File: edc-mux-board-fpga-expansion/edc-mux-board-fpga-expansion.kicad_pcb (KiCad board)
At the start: 4 copper layers, 224.5 x 177.5 mm, 375 parts, among them J1 DD-78F, J2 Device 8, J3 Device 9, J4 Device 10, J5 Device 11, J6 Device 12, J7 Device 13, J8 Device 14, J9 Device 15, U1 EP5358HUI, U10 TLV320AIC3206, U11 FSA2367, U12 P82B96, U13 TLV320AIC3206, U14 FSA2367, U15 P82B96, U16 TLV320AIC3206, U17 FSA2367, U18 P82B96, U19 TLV320AIC3206, U2 R-78B3.3-2.0, U20 FSA2367, U21 P82B96, U22 TLV320AIC3206, U23 FSA2367, U24 P82B96, U25 TLV320AIC3206, U26 FSA2367, U27 CDCLVC1108, U28 TCA9555RTWR, U29 TCA9548A, U3 P82B96, U4 TLV320AIC3206, U5 FSA2367, U6 P82B96, U7 TLV320AIC3206, U8 FSA2367, U9 P82B96

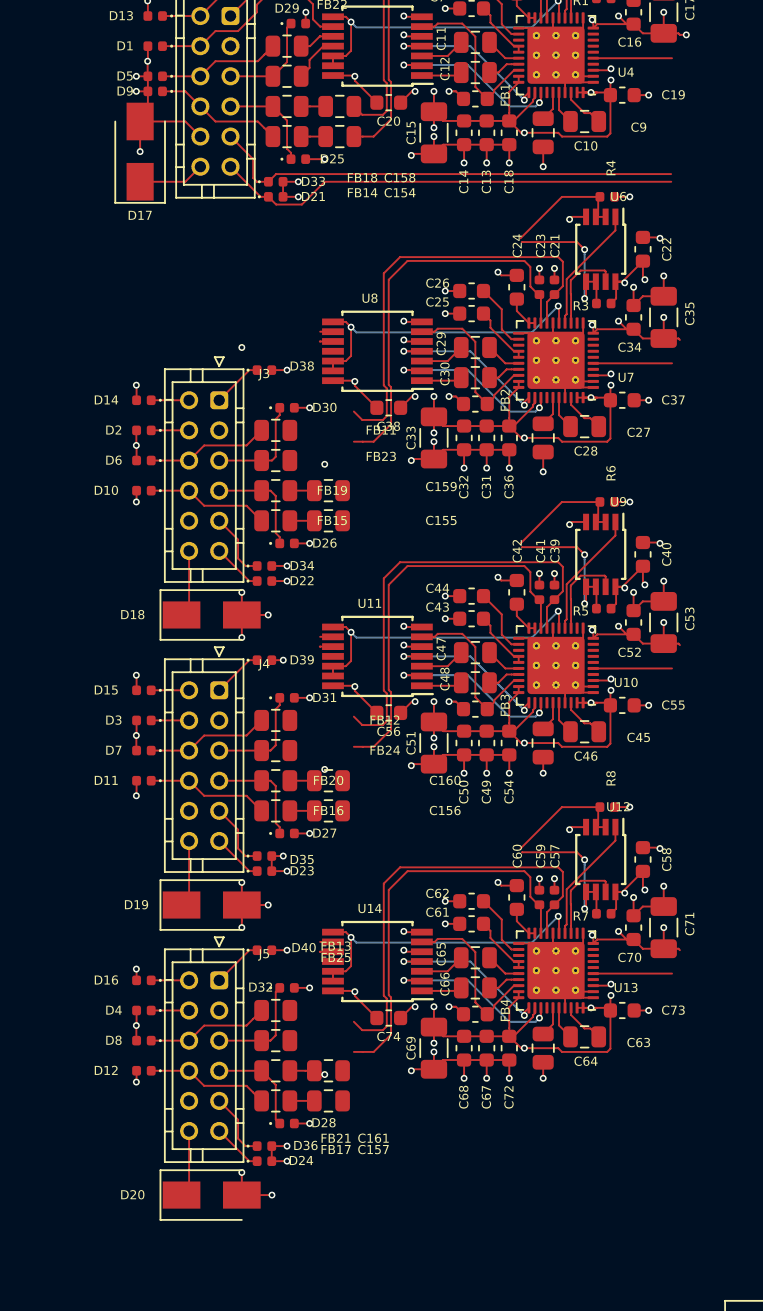
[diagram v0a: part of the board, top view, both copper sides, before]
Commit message: more pcb work. working on left side connector positioning
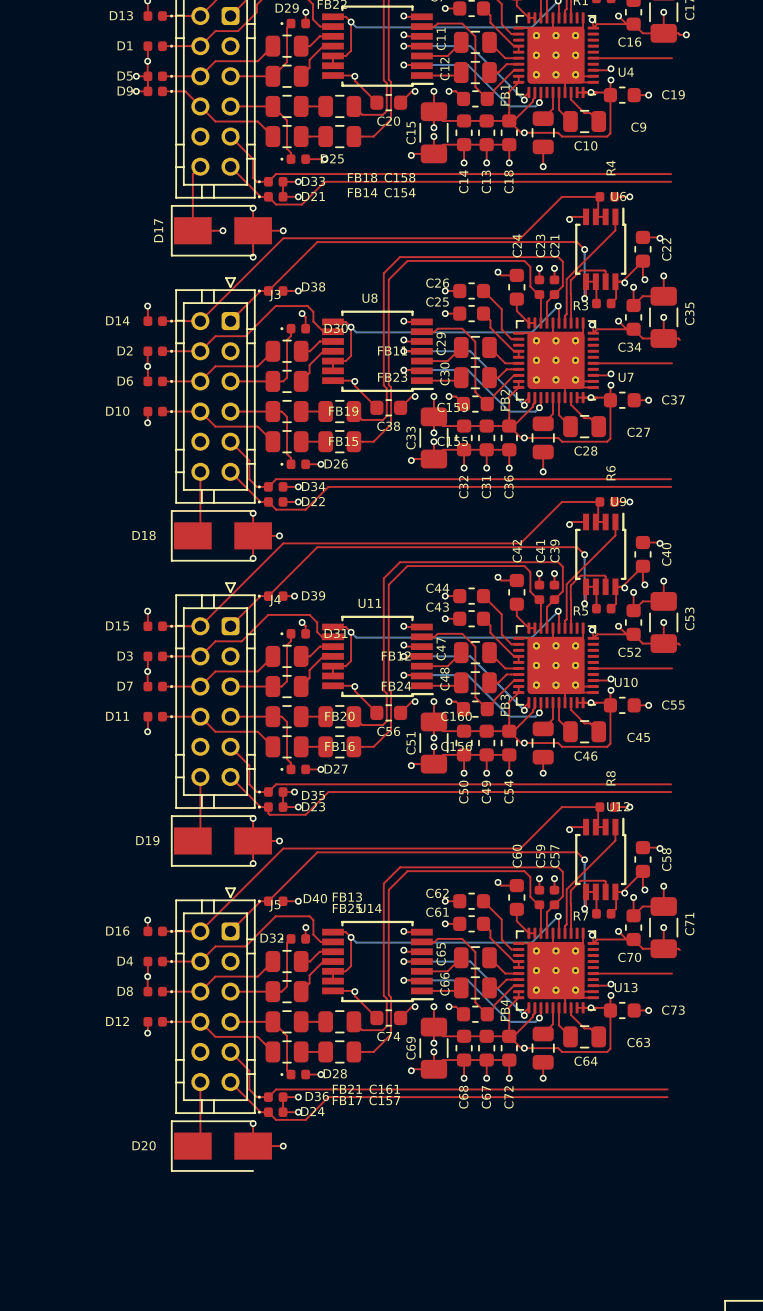
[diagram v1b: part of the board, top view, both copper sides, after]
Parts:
- moved D17 7.60 mm to (108.5, 64.8), turned to 0 degrees
- moved C155 5.30 mm to (116.2, 78.8)
- moved C159 5.30 mm to (116.2, 76.8)
- moved D10 5.30 mm to (104.0, 76.8)
- moved D14 5.30 mm to (104.0, 70.8)
- moved D18 5.30 mm to (108.5, 85.0)
- moved D2 5.30 mm to (104.0, 72.8)
- moved D22 5.30 mm to (112.0, 82.8)
- moved D26 5.30 mm to (113.5, 80.2)
- moved D30 5.30 mm to (113.5, 71.2)
- moved D34 5.30 mm to (112.0, 81.8)
- moved D38 5.30 mm to (112.0, 68.8)
- moved D6 5.30 mm to (104.0, 74.8)
- moved FB11 5.30 mm to (112.8, 72.8)
- moved FB15 5.30 mm to (112.8, 78.8)
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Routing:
- net /Left Side Connector Interconnects/ID_PIN10: track 3.34 -> 31.2 mm
- net /Left Side Connector Interconnects/ID_PIN9: track 3.34 -> 30.9 mm
- net /Left Side Connector Interconnects/ID_PIN11: track 3.34 -> 30.7 mm
- net /Left Side Connector Interconnects/INT_9: track 4.49 -> 31.4 mm
- net /Left Side Connector Interconnects/INT_10: track 4.49 -> 31.4 mm
- net /Left Side Connector Interconnects/INT_11: track 4.49 -> 31.2 mm
- net /CODEC interconnection sheet/SDA_HV9: track 10.8 -> 34.4 mm
- net /CODEC interconnection sheet/SDA_HV11: track 10.8 -> 34.4 mm
- net /CODEC interconnection sheet/SDA_HV10: track 10.8 -> 34.4 mm
- net /CODEC interconnection sheet/SCL_HV11: track 14.2 -> 32.4 mm
- net /CODEC interconnection sheet/SCL_HV10: track 14.2 -> 32.4 mm
- net /CODEC interconnection sheet/SCL_HV9: track 14.2 -> 32.4 mm
- net /CODEC interconnection sheet/AUD_GND11: track 3.37 -> 13.8 mm
- net /CODEC interconnection sheet/AUD_GND9: track 3.37 -> 13.6 mm
- net /CODEC interconnection sheet/AUD_GND10: track 3.37 -> 13.4 mm
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
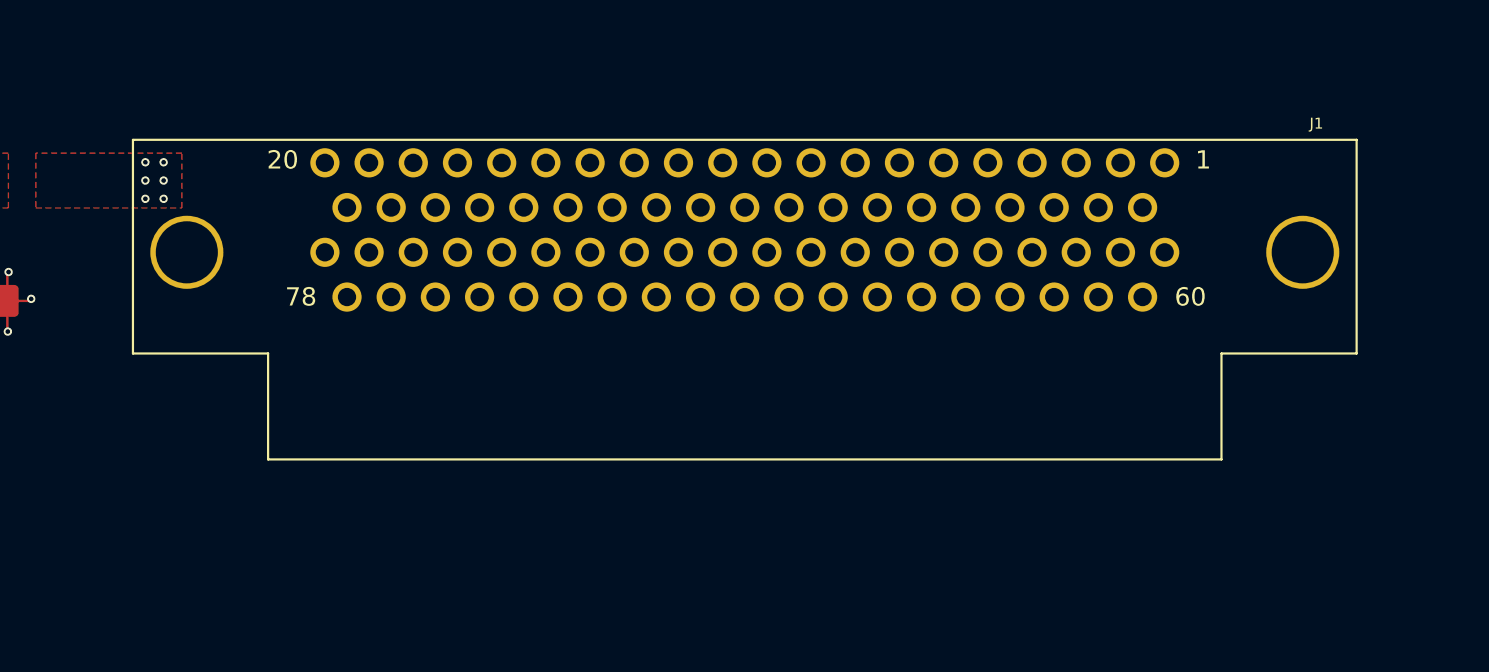
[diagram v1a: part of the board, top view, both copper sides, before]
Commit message: Changed expansion connector from DD-78 to DC-62
since the connector is literally half as much, and I don't need the extra pins
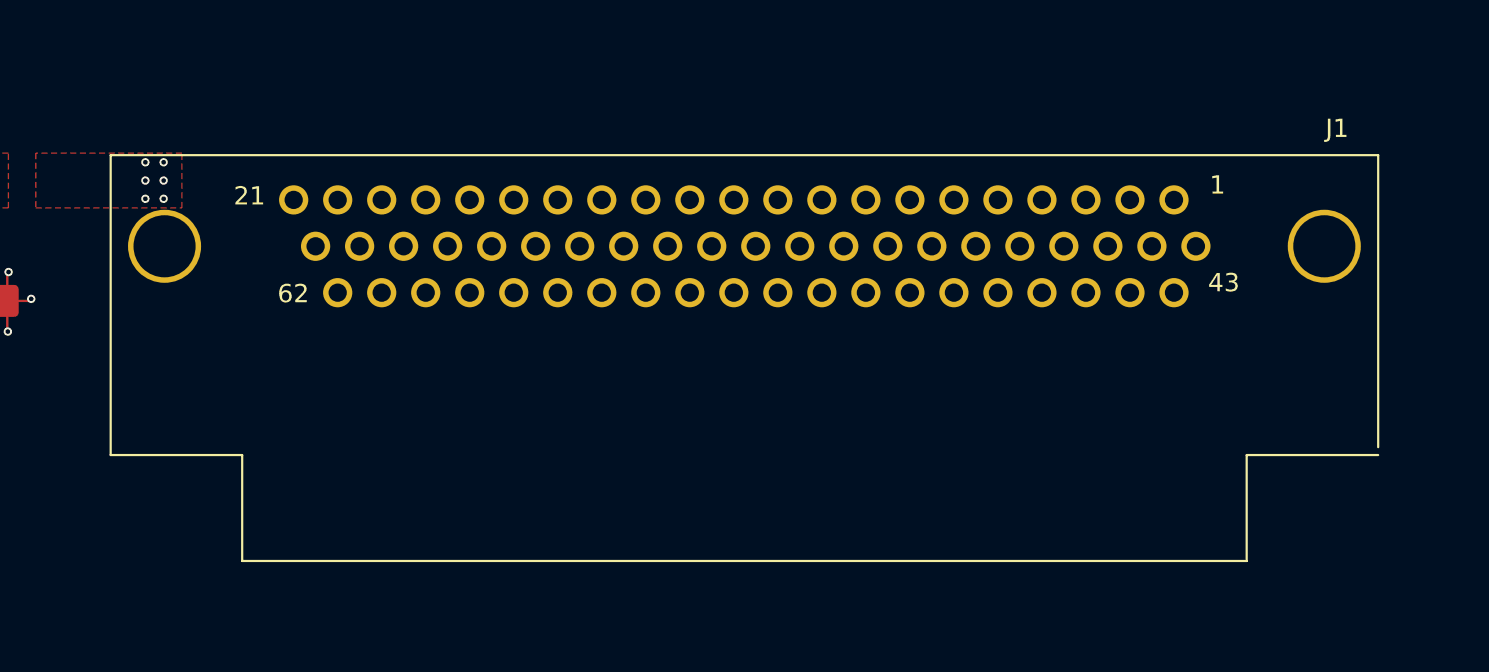
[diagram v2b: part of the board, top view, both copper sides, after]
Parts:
- J1: value DD-78F -> DC-62F; footprint SW-Harting:09565525612 -> SW-Harting:09564525612
- moved J1 2.78 mm to (175.3, 141.6)
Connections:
- J1 pad 1: (no net) -> Net-(J1-Pad1)
- J1 pad 10: (no net) -> Net-(J1-Pad10)
- J1 pad 11: (no net) -> Net-(J1-Pad11)
- J1 pad 12: (no net) -> Net-(J1-Pad12)
- J1 pad 13: (no net) -> Net-(J1-Pad13)
- J1 pad 14: (no net) -> Net-(J1-Pad14)
- J1 pad 15: (no net) -> Net-(J1-Pad15)
- J1 pad 16: (no net) -> Net-(J1-Pad16)
- J1 pad 17: (no net) -> Net-(J1-Pad17)
- J1 pad 18: (no net) -> Net-(J1-Pad18)
- J1 pad 19: (no net) -> Net-(J1-Pad19)
- J1 pad 2: (no net) -> Net-(J1-Pad2)
- J1 pad 20: (no net) -> Net-(J1-Pad20)
- J1 pad 21: (no net) -> Net-(J1-Pad21)
- J1 pad 22: (no net) -> Net-(J1-Pad22)
- J1 pad 23: (no net) -> Net-(J1-Pad23)
- J1 pad 24: (no net) -> Net-(J1-Pad24)
- J1 pad 25: (no net) -> Net-(J1-Pad25)
- J1 pad 26: (no net) -> Net-(J1-Pad26)
- J1 pad 27: (no net) -> Net-(J1-Pad27)
- J1 pad 28: (no net) -> Net-(J1-Pad28)
- J1 pad 29: (no net) -> Net-(J1-Pad29)
- J1 pad 3: (no net) -> Net-(J1-Pad3)
- J1 pad 30: (no net) -> Net-(J1-Pad30)
- J1 pad 31: (no net) -> Net-(J1-Pad31)
- J1 pad 32: (no net) -> Net-(J1-Pad32)
- J1 pad 33: (no net) -> Net-(J1-Pad33)
- J1 pad 34: (no net) -> Net-(J1-Pad34)
- J1 pad 35: (no net) -> Net-(J1-Pad35)
- J1 pad 36: (no net) -> Net-(J1-Pad36)
- J1 pad 37: (no net) -> Net-(J1-Pad37)
- J1 pad 38: (no net) -> Net-(J1-Pad38)
- J1 pad 39: (no net) -> Net-(J1-Pad39)
- J1 pad 4: (no net) -> Net-(J1-Pad4)
- J1 pad 40: (no net) -> Net-(J1-Pad40)
- J1 pad 41: (no net) -> Net-(J1-Pad41)
- J1 pad 42: (no net) -> Net-(J1-Pad42)
- J1 pad 43: (no net) -> Net-(J1-Pad43)
- J1 pad 44: (no net) -> Net-(J1-Pad44)
- J1 pad 45: (no net) -> Net-(J1-Pad45)
- J1 pad 46: (no net) -> Net-(J1-Pad46)
- J1 pad 47: (no net) -> Net-(J1-Pad47)
- J1 pad 48: (no net) -> Net-(J1-Pad48)
- J1 pad 49: (no net) -> Net-(J1-Pad49)
- J1 pad 5: (no net) -> Net-(J1-Pad5)
- J1 pad 50: (no net) -> Net-(J1-Pad50)
- J1 pad 51: (no net) -> Net-(J1-Pad51)
- J1 pad 52: (no net) -> Net-(J1-Pad52)
- J1 pad 53: (no net) -> Net-(J1-Pad53)
- J1 pad 54: (no net) -> Net-(J1-Pad54)
- J1 pad 55: (no net) -> Net-(J1-Pad55)
- J1 pad 56: (no net) -> Net-(J1-Pad56)
- J1 pad 57: (no net) -> Net-(J1-Pad57)
- J1 pad 58: (no net) -> Net-(J1-Pad58)
- J1 pad 59: (no net) -> Net-(J1-Pad59)
- J1 pad 6: (no net) -> Net-(J1-Pad6)
- J1 pad 60: (no net) -> Net-(J1-Pad60)
- J1 pad 61: (no net) -> Net-(J1-Pad61)
- J1 pad 62: (no net) -> Net-(J1-Pad62)
- J1 pad 7: (no net) -> Net-(J1-Pad7)
- J1 pad 8: (no net) -> Net-(J1-Pad8)
- J1 pad 9: (no net) -> Net-(J1-Pad9)

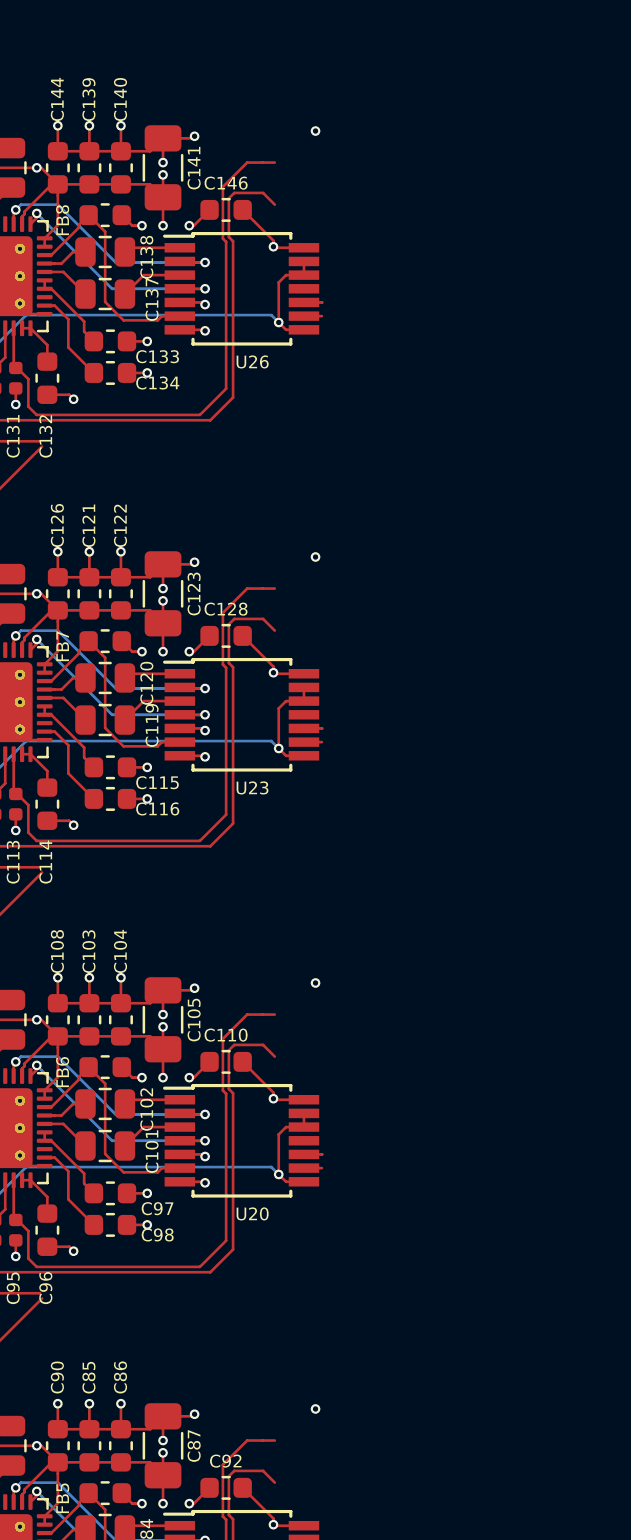
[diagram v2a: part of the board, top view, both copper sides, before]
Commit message: More work on expansion connector pinout connections
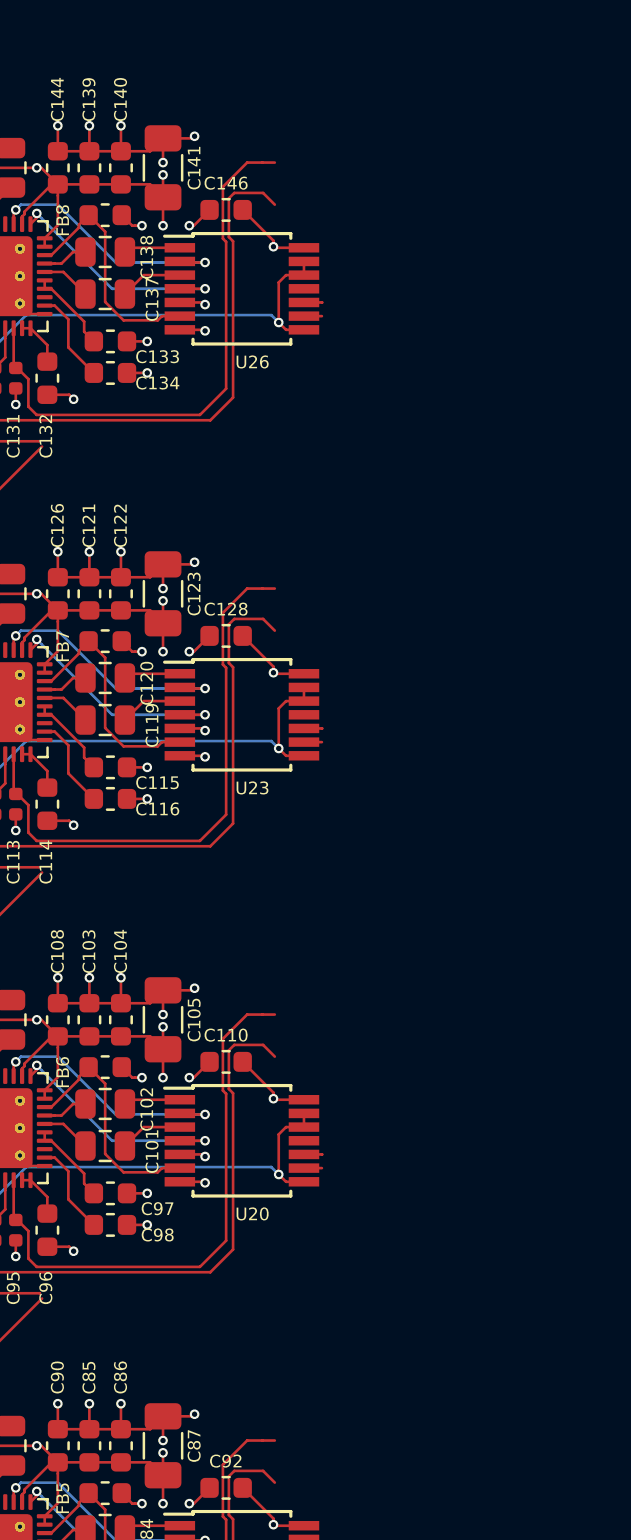
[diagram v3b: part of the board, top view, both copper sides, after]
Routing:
- net GND: vias 234 -> 230
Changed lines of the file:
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@@
     (thickness 1.6)
     (drawings 16)
-    (tracks 2785)
+    (tracks 2781)
     (zones 0)
     (modules 375)
@@
   (segment (start 234.55 55.65) (end 235.7 55.65) (width 0.127) (layer F.Cu) (net 1))
   (via (at 235.75 55.7) (size 0.4572) (drill 0.254) (layers F.Cu B.Cu) (net 1))
-  (via (at 241 46.2) (size 0.4572) (drill 0.254) (layers F.Cu B.Cu) (net 1))
   (segment (start 220.5 76.9875) (end 220.5 78.2) (width 0.127) (layer F.Cu) (net 1))
   (via (at 220.5 78.2) (size 0.4572) (drill 0.254) (layers F.Cu B.Cu) (net 1))
@@
   (segment (start 234.55 75.9) (end 235.7 75.9) (width 0.127) (layer F.Cu) (net 1))
   (via (at 235.75 75.95) (size 0.4572) (drill 0.254) (layers F.Cu B.Cu) (net 1))
-  (via (at 241 66.45) (size 0.4572) (drill 0.254) (layers F.Cu B.Cu) (net 1))
   (segment (start 220.5 97.2375) (end 220.5 98.45) (width 0.127) (layer F.Cu) (net 1))
   (via (at 220.5 98.45) (size 0.4572) (drill 0.254) (layers F.Cu B.Cu) (net 1))
@@
   (segment (start 234.55 96.15) (end 235.7 96.15) (width 0.127) (layer F.Cu) (net 1))
   (via (at 235.75 96.2) (size 0.4572) (drill 0.254) (layers F.Cu B.Cu) (net 1))
-  (via (at 241 86.7) (size 0.4572) (drill 0.254) (layers F.Cu B.Cu) (net 1))
   (segment (start 220.5 117.4875) (end 220.5 118.7) (width 0.127) (layer F.Cu) (net 1))
   (via (at 220.5 118.7) (size 0.4572) (drill 0.254) (layers F.Cu B.Cu) (net 1))
@@
   (segment (start 234.55 116.4) (end 235.7 116.4) (width 0.127) (layer F.Cu) (net 1))
   (via (at 235.75 116.45) (size 0.4572) (drill 0.254) (layers F.Cu B.Cu) (net 1))
-  (via (at 241 106.95) (size 0.4572) (drill 0.254) (layers F.Cu B.Cu) (net 1))
   (segment (start 135.75 110.2125) (end 135.75 109) (width 0.127) (layer F.Cu) (net 1))
   (via (at 135.75 109) (size 0.4572) (drill 0.254) (layers F.Cu B.Cu) (net 1))
